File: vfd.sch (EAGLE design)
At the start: 41 parts, among them J1 KEYPAD, J3 ARDUINO_R3, U1 20070-1A04PTH, X1 DRV

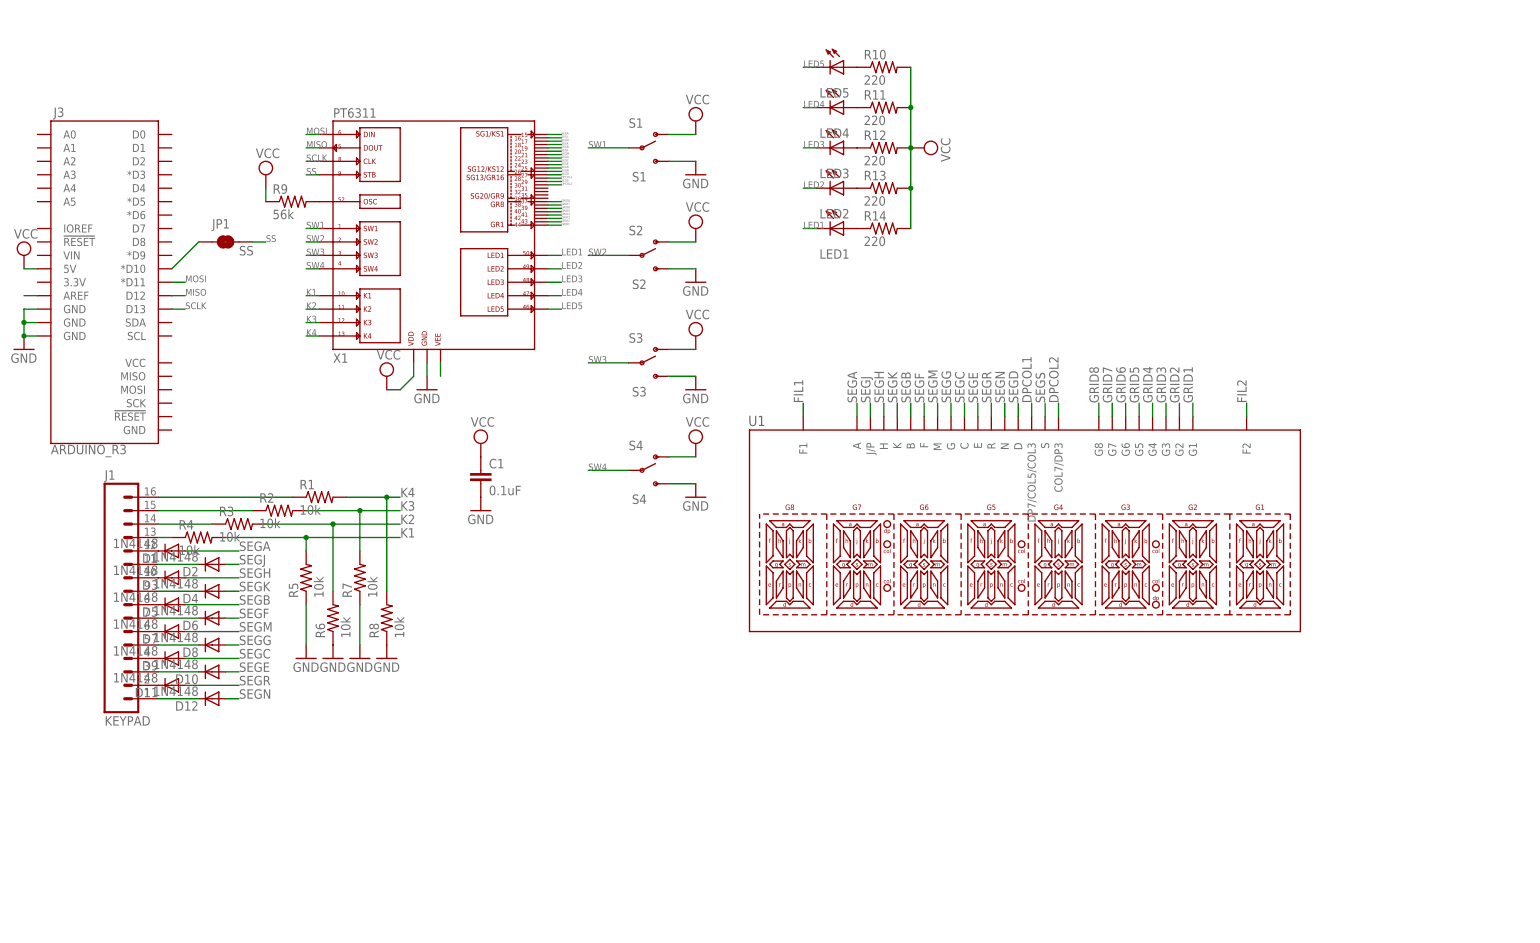
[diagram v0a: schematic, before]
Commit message: add filament driver components
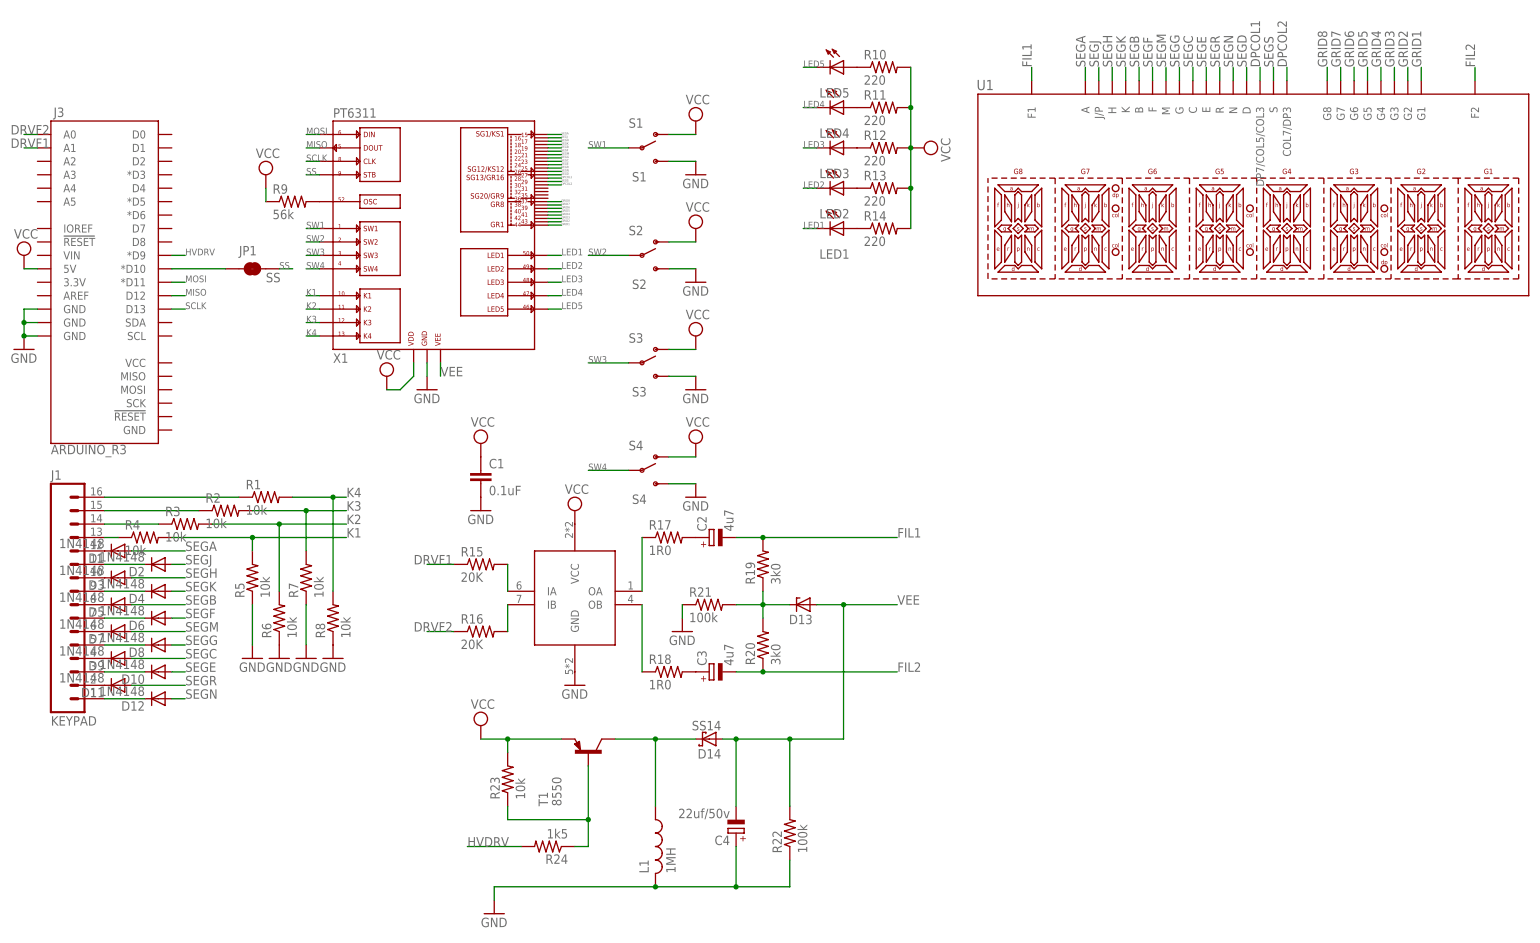
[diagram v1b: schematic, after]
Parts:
- added C2, C3: 4u7, resistor:CPOL-EUB45181A
- added C4: 22uf/50v, resistor:CPOL-EUB45181A
- added D13: (no value), diode:ZENER-DIODEZD-12.5
- added D14: SS14, diode:SCHOTTKY-DIODEF126Z12
- added L1: 1MH, resistor:L-US0204/5
- added R15, R16: 20K, resistor:R-US_0204/5
- added R17, R18: 1R0, resistor:R-US_0204/5
- added R19, R20: 3k0, resistor:R-US_0204/7
- added R21: 100k, resistor:R-US_0204/7
- added R22: 100k, resistor:R-US_0204/5
- added R23: 10k, resistor:R-US_0204/5
- added R24: 1k5, resistor:R-US_0204/5
- added T1: 8550, transistor:-PNP-TO92
- added U$1: L9110, Drivers:L9110
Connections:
- removed net N$14: X1.VEE
- removed net N$19: J3.AREF
- new net DRVF1: J3.A1, R15.1
- new net DRVF2: J3.A0, R16.1
- new net HVDRV: J3.*D9, R24.2
- new net N$26: R15.2, U$1.IA
- new net N$27: R16.2, U$1.IB
- new net N$28: R17.1, U$1.OA
- new net N$29: R18.1, U$1.OB
- new net N$30: C2.+, R17.2
- new net N$31: C3.+, R18.2
- new net N$35: D13.C, R19.1, R20.2, R21.2
- new net N$36: R23.1, R24.1, T1.B
- new net N$40: D14.C, L1.1, T1.C
- new net VEE: C4.-, D13.A, D14.A, R22.2, X1.VEE
- net FIL1: now also C2.-, R19.2
- net FIL2: now also C3.-, R20.1
- net GND: now also C4.+, L1.2, R21.1, R22.1, U$1.GND
- net VCC: now also R23.2, T1.E, U$1.VCC
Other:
- moved on the sheet: D1, D10, D11, D12, D2, D3, D4, D5, D6, D7, D8, D9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

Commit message: all lines laid
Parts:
- D13: device diode:ZENER-DIODEZD-12.5 -> diode:ZENER-DIODEDO34-7
- D14: device diode:SCHOTTKY-DIODEF126Z12 -> diode:SCHOTTKY-DIODEDO35-7
- R5, R6, R7, R8: device resistor:R-US_0204/7 -> resistor:R-US_0204/5
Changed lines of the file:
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@@
 <part name="R4" library="resistor" deviceset="R-US_" device="0204/7" value="10k"/>
 <part name="GND1" library="supply1" deviceset="GND" device=""/>
-<part name="R5" library="resistor" deviceset="R-US_" device="0204/7" value="10k"/>
-<part name="R6" library="resistor" deviceset="R-US_" device="0204/7" value="10k"/>
-<part name="R7" library="resistor" deviceset="R-US_" device="0204/7" value="10k"/>
-<part name="R8" library="resistor" deviceset="R-US_" device="0204/7" value="10k"/>
+<part name="R5" library="resistor" deviceset="R-US_" device="0204/5" value="10k"/>
+<part name="R6" library="resistor" deviceset="R-US_" device="0204/5" value="10k"/>
+<part name="R7" library="resistor" deviceset="R-US_" device="0204/5" value="10k"/>
+<part name="R8" library="resistor" deviceset="R-US_" device="0204/5" value="10k"/>
 <part name="GND2" library="supply1" deviceset="GND" device=""/>
 <part name="GND3" library="supply1" deviceset="GND" device=""/>
@@
 <part name="R21" library="resistor" deviceset="R-US_" device="0204/7" value="100k"/>
 <part name="GND13" library="supply1" deviceset="GND" device=""/>
-<part name="D13" library="diode" deviceset="ZENER-DIODE" device="ZD-12.5"/>
+<part name="D13" library="diode" deviceset="ZENER-DIODE" device="DO34-7"/>
 <part name="R20" library="resistor" deviceset="R-US_" device="0204/7" value="3k0"/>
-<part name="D14" library="diode" deviceset="SCHOTTKY-DIODE" device="F126Z12" value="SS14"/>
+<part name="D14" library="diode" deviceset="SCHOTTKY-DIODE" device="DO35-7" value="SS14"/>
 <part name="C4" library="resistor" deviceset="CPOL-EU" device="B45181A" value="22uf/50v"/>
 <part name="R22" library="resistor" deviceset="R-US_" device="0204/5" value="100k"/>
